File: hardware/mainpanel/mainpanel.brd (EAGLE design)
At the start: 80 x 80 mm, 9 parts, among them J1 90136-106, J2 90136-104, J3 90136-104, J4 90136-108, J5 90136-104

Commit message: Add values for parts
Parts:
- B1: value (none) -> NUCLEO-32
- B3: value (none) -> UPUTRONICS-UBLOX-PICO
- B4: value (none) -> SPARKFUN-OPENLOG
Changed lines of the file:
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@@
 <param name="RoutingGrid" value="0.125mm"/>
 <param name="AutoGrid" value="1"/>
-<param name="Efforts" value="1"/>
+<param name="Efforts" value="2"/>
 <param name="TopRouterVariant" value="1"/>
 <param name="tpViaShape" value="round"/>
@@
 </autorouter>
 <elements>
-<element name="B1" library="Frcy" package="NUCLEO-32" value="" x="47.4" y="36.86" rot="R270"/>
+<element name="B1" library="Frcy" package="NUCLEO-32" value="NUCLEO-32" x="47.4" y="36.86" rot="R270"/>
 <element name="B2" library="Frcy" package="BOSCH-BNO055" value="BOSCH-BNO055" x="39.67" y="15.77" rot="R180"/>
-<element name="B3" library="Frcy" package="UPUTRONICS-UBLOX-PICO" value="" x="58" y="48"/>
-<element name="B4" library="Frcy" package="SPARKFUN-OPENLOG" value="" x="66" y="16" rot="R180"/>
+<element name="B3" library="Frcy" package="UPUTRONICS-UBLOX-PICO" value="UPUTRONICS-UBLOX-PICO" x="58" y="48"/>
+<element name="B4" library="Frcy" package="SPARKFUN-OPENLOG" value="SPARKFUN-OPENLOG" x="66" y="16" rot="R180"/>
 <element name="J2" library="con-molex-c-grid" package="90136-1?04" value="90136-104" x="34" y="72"/>
 <element name="J3" library="con-molex-c-grid" package="90136-1?04" value="90136-104" x="50" y="72"/>

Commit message: Move parts on sch
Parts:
- B2: value BOSCH-BNO055 -> BNO055
- B3: value UPUTRONICS-UBLOX-PICO -> UBLOX
- B4: value SPARKFUN-OPENLOG -> OPENLOG
- J1: value 90136-106 -> CDH
- J2: value 90136-104 -> OW
- J3: value 90136-104 -> DBG
- J4: value 90136-108 -> EXT
- J5: value 90136-104 -> SUN
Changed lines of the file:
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@@
 <elements>
 <element name="B1" library="Frcy" package="NUCLEO-32" value="NUCLEO-32" x="47.4" y="36.86" rot="R270"/>
-<element name="B2" library="Frcy" package="BOSCH-BNO055" value="BOSCH-BNO055" x="39.67" y="15.77" rot="R180"/>
-<element name="B3" library="Frcy" package="UPUTRONICS-UBLOX-PICO" value="UPUTRONICS-UBLOX-PICO" x="58" y="48"/>
-<element name="B4" library="Frcy" package="SPARKFUN-OPENLOG" value="SPARKFUN-OPENLOG" x="66" y="16" rot="R180"/>
-<element name="J2" library="con-molex-c-grid" package="90136-1?04" value="90136-104" x="34" y="72"/>
-<element name="J3" library="con-molex-c-grid" package="90136-1?04" value="90136-104" x="50" y="72"/>
-<element name="J1" library="con-molex-c-grid" package="90136-1?06" value="90136-106" x="15" y="72"/>
-<element name="J4" library="con-molex-c-grid" package="90136-1?08" value="90136-108" x="10" y="28" rot="R90"/>
-<element name="J5" library="con-molex-c-grid" package="90136-1?04" value="90136-104" x="10" y="51" rot="R270"/>
+<element name="B2" library="Frcy" package="BOSCH-BNO055" value="BNO055" x="39.67" y="15.77" rot="R180"/>
+<element name="B3" library="Frcy" package="UPUTRONICS-UBLOX-PICO" value="UBLOX" x="58" y="48"/>
+<element name="B4" library="Frcy" package="SPARKFUN-OPENLOG" value="OPENLOG" x="66" y="16" rot="R180"/>
+<element name="J2" library="con-molex-c-grid" package="90136-1?04" value="OW" x="34" y="72"/>
+<element name="J3" library="con-molex-c-grid" package="90136-1?04" value="DBG" x="50" y="72"/>
+<element name="J1" library="con-molex-c-grid" package="90136-1?06" value="CDH" x="15" y="72"/>
+<element name="J4" library="con-molex-c-grid" package="90136-1?08" value="EXT" x="10" y="28" rot="R90"/>
+<element name="J5" library="con-molex-c-grid" package="90136-1?04" value="SUN" x="10" y="51" rot="R270"/>
 </elements>
 <signals>

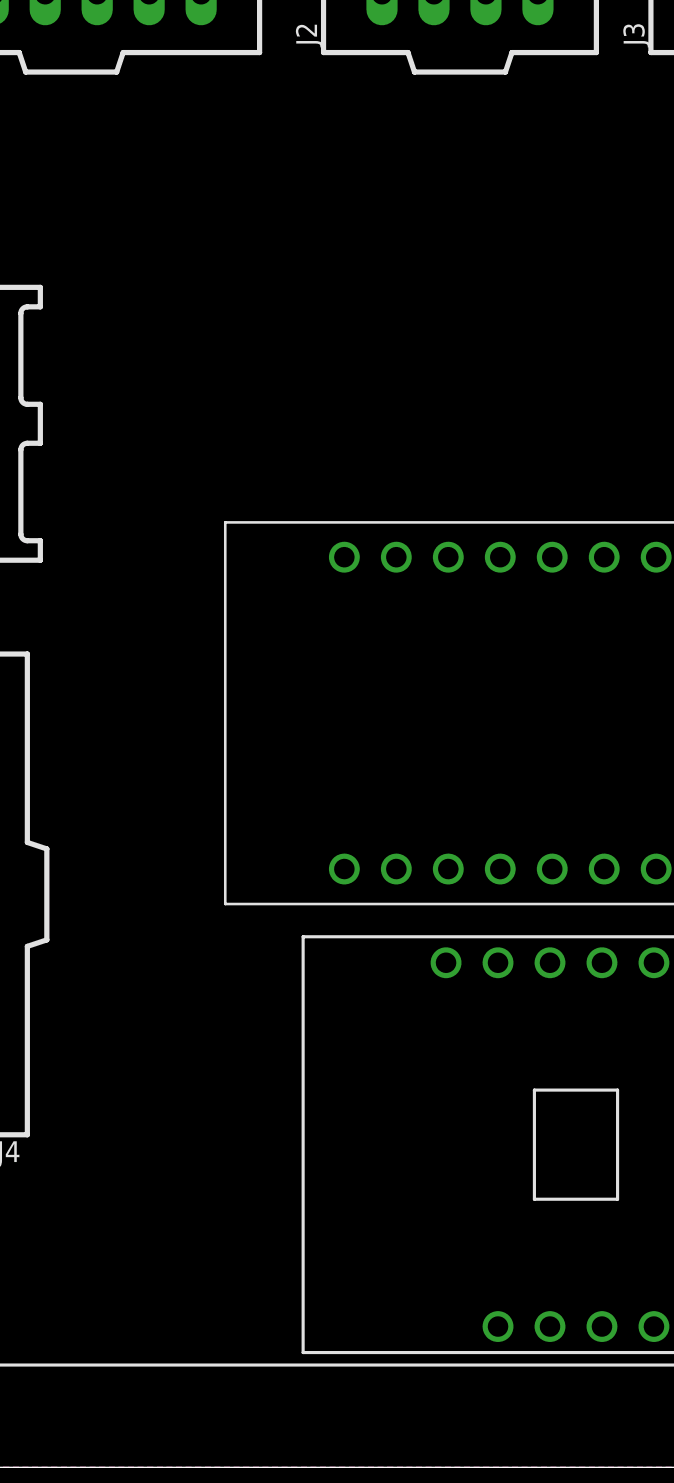
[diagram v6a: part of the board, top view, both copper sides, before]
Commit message: Add DS18B20 sensors
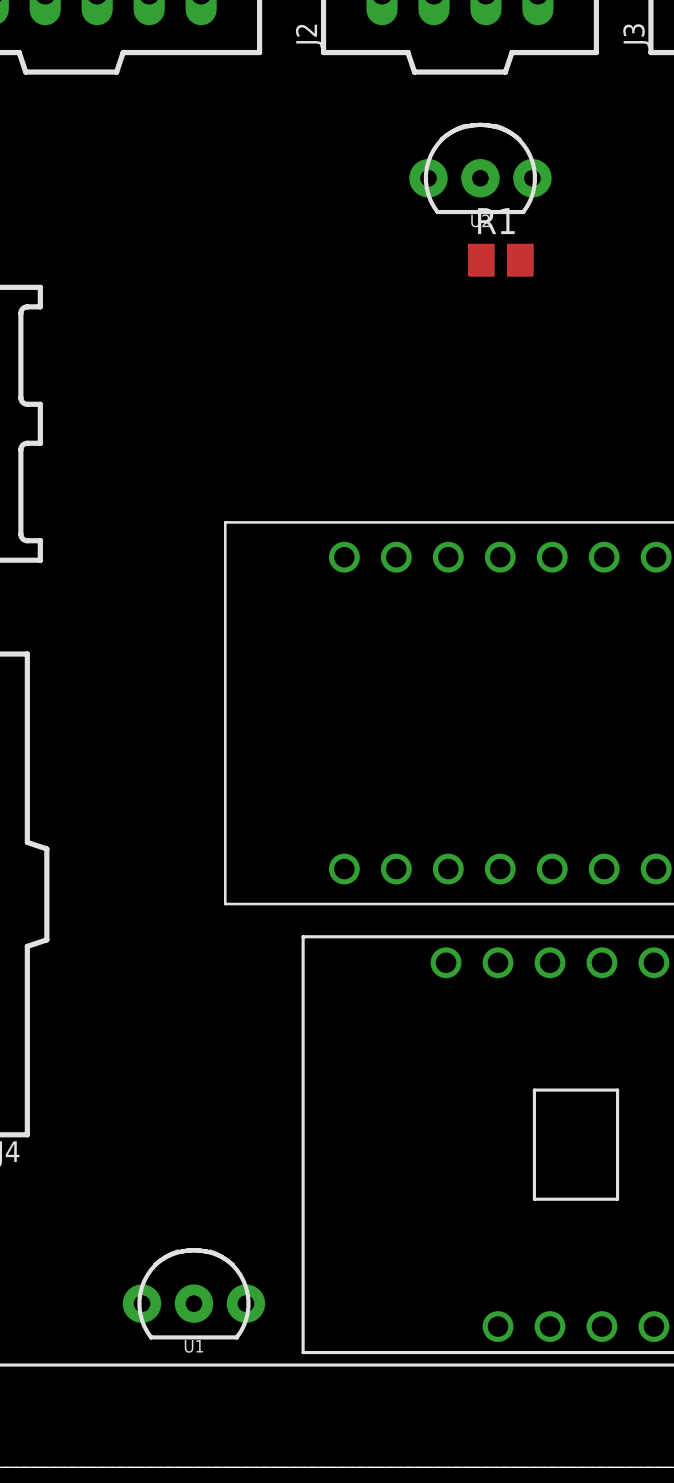
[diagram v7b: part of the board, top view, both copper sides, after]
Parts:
- added R1: 4.7k, resistor:M2012
- added U1, U2: DS18B20, Frcy:TO-92-AMMO
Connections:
- net GND: now also J2.2, U1.1, U2.1; no longer J2.3
- net TEMP-OW: now also J2.3, R1.1, U1.2, U2.2; no longer J2.2
- net VCC: now also R1.2, U1.3, U2.3
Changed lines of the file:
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@@
 <element name="J4" library="con-molex-c-grid" package="90136-1?08" value="EXT" x="10" y="28" rot="R90"/>
 <element name="J5" library="con-molex-c-grid" package="90136-1?04" value="SUN" x="10" y="51" rot="R270"/>
+<element name="R1" library="resistor" library_urn="urn:adsk.eagle:library:348" package="M2012" package3d_urn="urn:adsk.eagle:package:26082/1" value="4.7k" x="36" y="59"/>
+<element name="U1" library="Frcy" package="TO-92-AMMO" value="DS18B20" x="21" y="8">
+<attribute name="STORE_ID" value="SEN-00245" x="21" y="8" size="1.778" layer="27" display="off"/>
+</element>
+<element name="U2" library="Frcy" package="TO-92-AMMO" value="DS18B20" x="35" y="63">
+<attribute name="STORE_ID" value="SEN-00245" x="35" y="63" size="1.778" layer="27" display="off"/>
+</element>
 </elements>
 <signals>
@@
 <contactref element="J4" pad="8"/>
 <contactref element="J5" pad="4"/>
+<contactref element="U1" pad="3"/>
+<contactref element="U2" pad="3"/>
+<contactref element="R1" pad="2"/>
 <wire x1="64.73" y1="24.128" x2="71.97" y2="49.27" width="0" layer="19" extent="1-1"/>
 <wire x1="46.02" y1="24.66" x2="64.73" y2="24.128" width="0" layer="19" extent="1-1"/>
@@
 <wire x1="10" y1="36.89" x2="30.89" y2="29.24" width="0" layer="19" extent="1-1"/>
 <wire x1="10" y1="47.19" x2="10" y2="36.89" width="0" layer="19" extent="1-1"/>
+<wire x1="23.54" y1="8" x2="30.89" y2="29.24" width="0" layer="19" extent="1-1"/>
 <wire x1="11.19" y1="72" x2="10" y2="47.19" width="0" layer="19" extent="1-1"/>
 <wire x1="37.81" y1="72" x2="11.19" y2="72" width="0" layer="19" extent="1-1"/>
+<wire x1="37.54" y1="63" x2="37.81" y2="72" width="0" layer="19" extent="1-1"/>
+<wire x1="36.95" y1="59" x2="37.54" y2="63" width="0" layer="19" extent="1-1"/>
 </signal>
 <signal name="GND">
@@
 <contactref element="B4" pad="GND"/>
 <contactref element="J2" pad="1"/>
-<contactref element="J2" pad="3"/>
 <contactref element="J1" pad="1"/>
 <contactref element="J1" pad="5"/>
@@
 <contactref element="J4" pad="5"/>
 <contactref element="J5" pad="1"/>
+<contactref element="J2" pad="2"/>
+<contactref element="U1" pad="1"/>
+<contactref element="U2" pad="1"/>
 </signal>
 <signal name="IMU-SDA">
@@
 <signal name="TEMP-OW">
 <contactref element="B1" pad="D9"/>
-<contactref element="J2" pad="2"/>
-<wire x1="35.97" y1="44.48" x2="32.73" y2="72" width="0" layer="19" extent="1-1"/>
+<contactref element="J2" pad="3"/>
+<contactref element="U1" pad="2"/>
+<contactref element="U2" pad="2"/>
+<contactref element="R1" pad="1"/>
+<wire x1="35" y1="63" x2="35.27" y2="72" width="0" layer="19" extent="1-1"/>
+<wire x1="35.05" y1="59" x2="35" y2="63" width="0" layer="19" extent="1-1"/>
+<wire x1="35.97" y1="44.48" x2="35.05" y2="59" width="0" layer="19" extent="1-1"/>
+<wire x1="21" y1="8" x2="35.97" y2="44.48" width="0" layer="19" extent="1-1"/>
 </signal>
 <signal name="SPI-SCK">
@@
 </board>
 </drawing>
+<compatibility>
+<note version="8.2" severity="warning">
+Since Version 8.2, EAGLE supports online libraries. The ids
+of those online libraries will not be understood (or retained)
+with this version.
+</note>
+<note version="8.3" severity="warning">
+Since Version 8.3, EAGLE supports URNs for individual library
+assets (packages, symbols, and devices). The URNs of those assets
+will not be understood (or retained) with this version.
+</note>
+<note version="8.3" severity="warning">
+Since Version 8.3, EAGLE supports the association of 3D packages
+with devices in libraries, schematics, and board files. Those 3D
+packages will not be understood (or retained) with this version.
+</note>
+</compatibility>
 </eagle>

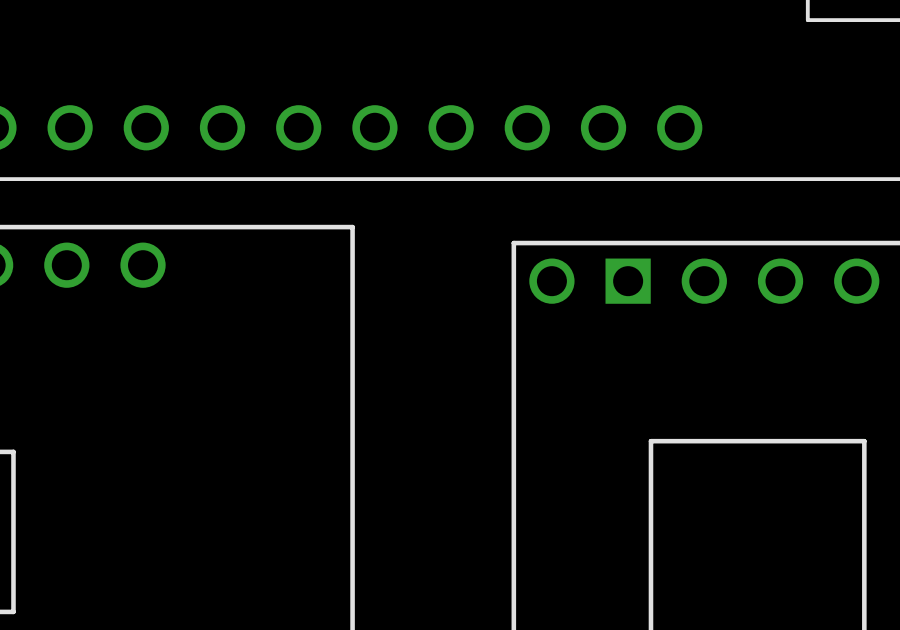
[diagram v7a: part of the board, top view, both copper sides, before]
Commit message: Set rst pin to vcc
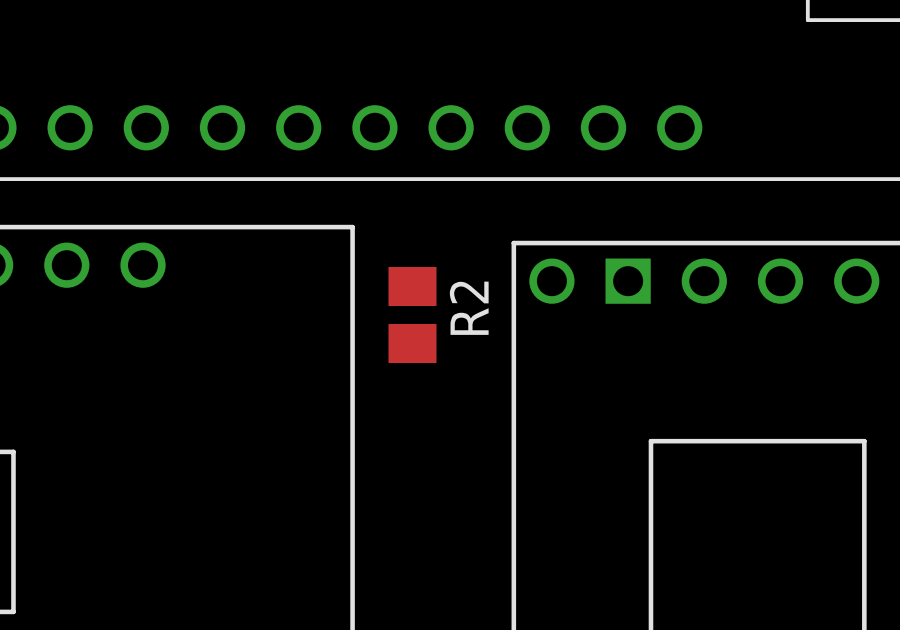
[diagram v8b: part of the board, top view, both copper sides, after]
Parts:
- added R2: 4.7k, resistor:M2012
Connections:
- removed net N$13: B1.RST@2
- new net N$1: B1.RST@2, R2.1
- net VCC: now also R2.2
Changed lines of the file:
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@@
 <attribute name="STORE_ID" value="SEN-00245" x="35" y="63" size="1.778" layer="27" display="off"/>
 </element>
+<element name="R2" library="resistor" library_urn="urn:adsk.eagle:library:348" package="M2012" package3d_urn="urn:adsk.eagle:package:26082/1" value="4.7k" x="55" y="23" rot="R270"/>
 </elements>
 <signals>
@@
 <contactref element="U2" pad="3"/>
 <contactref element="R1" pad="2"/>
+<contactref element="R2" pad="2"/>
 <wire x1="64.73" y1="24.128" x2="71.97" y2="49.27" width="0" layer="19" extent="1-1"/>
 <wire x1="46.02" y1="24.66" x2="64.73" y2="24.128" width="0" layer="19" extent="1-1"/>
@@
 <wire x1="10" y1="47.19" x2="10" y2="36.89" width="0" layer="19" extent="1-1"/>
 <wire x1="23.54" y1="8" x2="30.89" y2="29.24" width="0" layer="19" extent="1-1"/>
+<wire x1="55" y1="22.05" x2="23.54" y2="8" width="0" layer="19" extent="1-1"/>
 <wire x1="11.19" y1="72" x2="10" y2="47.19" width="0" layer="19" extent="1-1"/>
 <wire x1="37.81" y1="72" x2="11.19" y2="72" width="0" layer="19" extent="1-1"/>
@@
 <contactref element="B1" pad="VIN"/>
 </signal>
-<signal name="N$13">
-<contactref element="B1" pad="RST@2"/>
-</signal>
 <signal name="GPS-TX">
 <contactref element="B3" pad="TXD"/>
@@
 <wire x1="10" y1="49.73" x2="43.59" y2="29.24" width="0" layer="19" extent="1-1"/>
 </signal>
+<signal name="N$1">
+<contactref element="B1" pad="RST@2"/>
+<contactref element="R2" pad="1"/>
+<wire x1="55" y1="23.95" x2="58.83" y2="29.24" width="0" layer="19" extent="1-1"/>
+</signal>
 </signals>
